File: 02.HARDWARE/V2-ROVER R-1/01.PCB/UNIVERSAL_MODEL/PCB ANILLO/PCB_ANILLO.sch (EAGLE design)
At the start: 2 parts

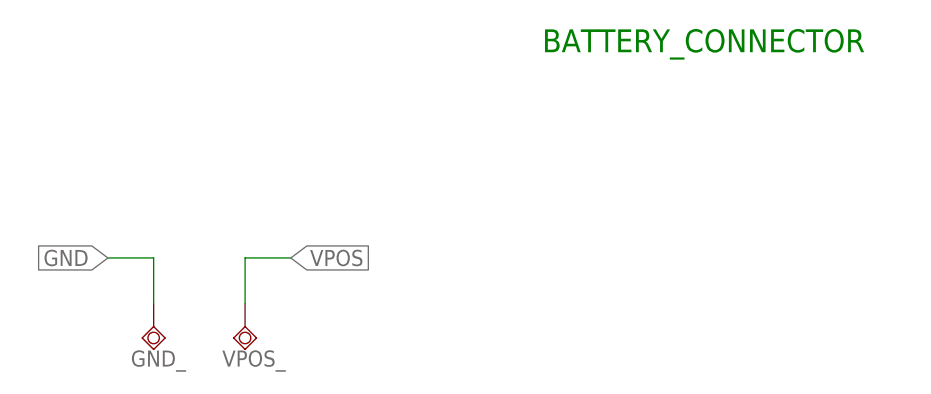
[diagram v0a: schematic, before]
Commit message: Cambio de  diseño de las placas de la univerasl
v2
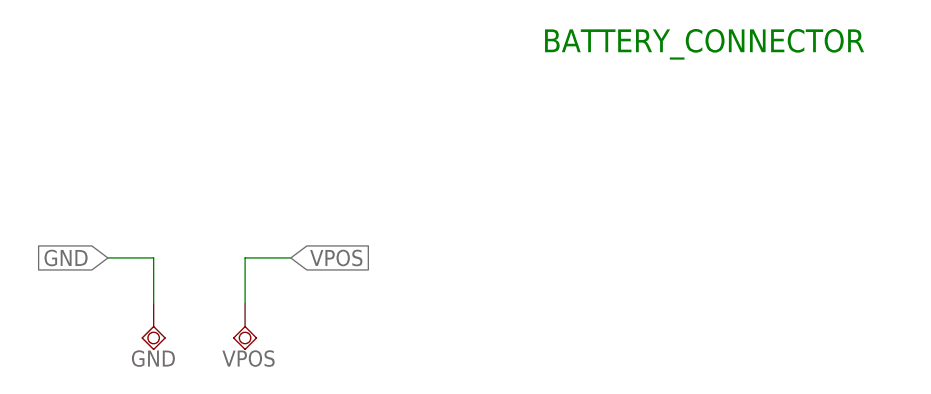
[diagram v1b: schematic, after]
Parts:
- renumbered GND_ to GND, VPOS_ to VPOS
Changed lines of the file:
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@@
 </classes>
 <parts>
-<part name="GND_" library="BeagleBone_Blue_R3" library_urn="urn:adsk.eagle:library:5828899" deviceset="TESTPAD_TPSQ" device="B1,27" package3d_urn="urn:adsk.eagle:package:5829773/2"/>
-<part name="VPOS_" library="BeagleBone_Blue_R3" library_urn="urn:adsk.eagle:library:5828899" deviceset="TESTPAD_TPSQ" device="B1,27" package3d_urn="urn:adsk.eagle:package:5829773/2"/>
+<part name="GND" library="BeagleBone_Blue_R3" library_urn="urn:adsk.eagle:library:5828899" deviceset="TESTPAD_TPSQ" device="B1,27" package3d_urn="urn:adsk.eagle:package:5829773/2"/>
+<part name="VPOS" library="BeagleBone_Blue_R3" library_urn="urn:adsk.eagle:library:5828899" deviceset="TESTPAD_TPSQ" device="B1,27" package3d_urn="urn:adsk.eagle:package:5829773/2"/>
 </parts>
 <sheets>
@@
 </plain>
 <instances>
-<instance part="GND_" gate="G$1" x="15.24" y="76.2" smashed="yes">
+<instance part="GND" gate="G$1" x="15.24" y="76.2" smashed="yes">
 <attribute name="NAME" x="12.7" y="71.755" size="1.778" layer="95"/>
 <attribute name="TP_SIGNAL_NAME" x="17.78" y="74.93" size="1.778" layer="97"/>
 </instance>
-<instance part="VPOS_" gate="G$1" x="25.4" y="76.2" smashed="yes">
+<instance part="VPOS" gate="G$1" x="25.4" y="76.2" smashed="yes">
 <attribute name="NAME" x="22.86" y="71.755" size="1.778" layer="95"/>
 <attribute name="TP_SIGNAL_NAME" x="27.94" y="74.93" size="1.778" layer="97"/>
@@
 <net name="GND" class="0">
 <segment>
-<pinref part="GND_" gate="G$1" pin="TP"/>
+<pinref part="GND" gate="G$1" pin="TP"/>
 <wire x1="15.24" y1="78.74" x2="15.24" y2="83.82" width="0.1524" layer="91"/>
 <wire x1="15.24" y1="83.82" x2="10.16" y2="83.82" width="0.1524" layer="91"/>
@@
 <net name="VPOS" class="0">
 <segment>
-<pinref part="VPOS_" gate="G$1" pin="TP"/>
+<pinref part="VPOS" gate="G$1" pin="TP"/>
 <wire x1="25.4" y1="78.74" x2="25.4" y2="83.82" width="0.1524" layer="91"/>
 <wire x1="25.4" y1="83.82" x2="30.48" y2="83.82" width="0.1524" layer="91"/>
